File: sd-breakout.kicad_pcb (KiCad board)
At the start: 2 copper layers, 31.1 x 27.9 mm, 7 parts, among them J1 Header, J2 microSD Socket, U1 EClamp2410P

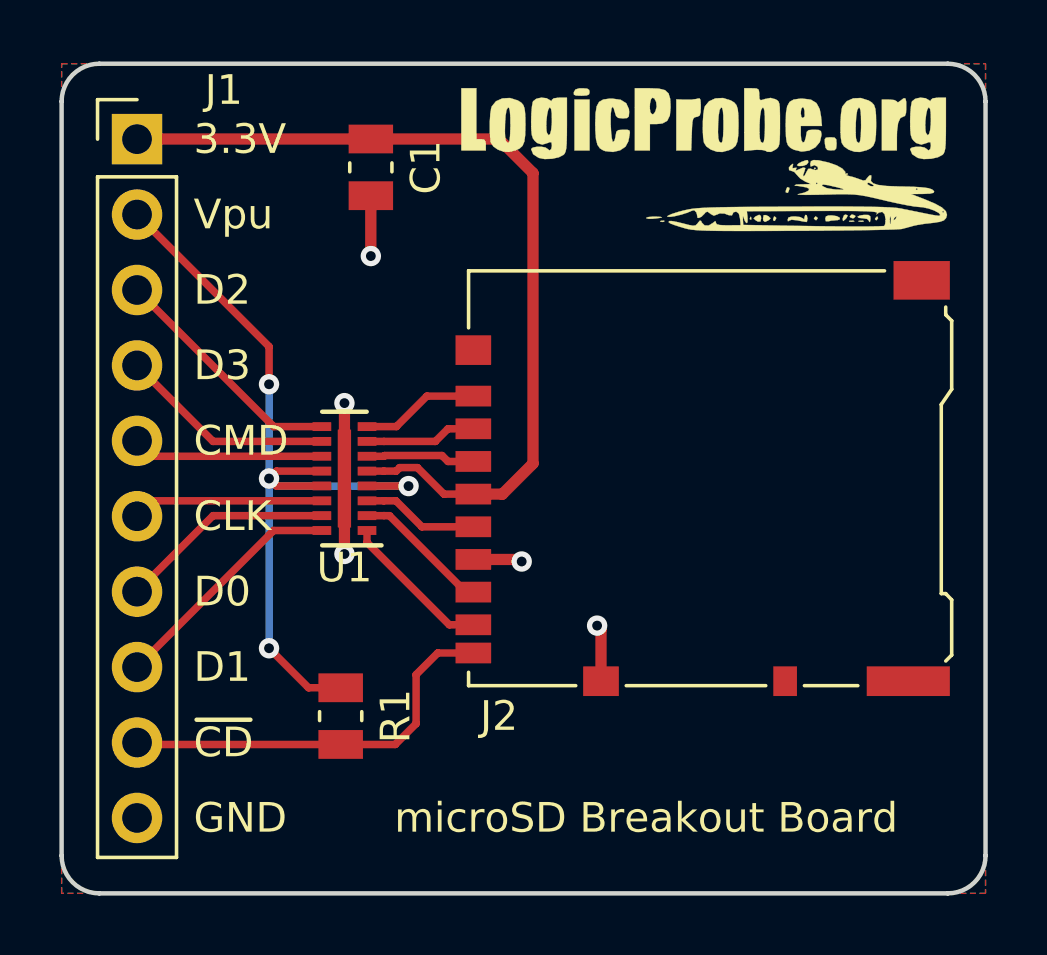
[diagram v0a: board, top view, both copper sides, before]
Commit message: Updated project to KiCad v6
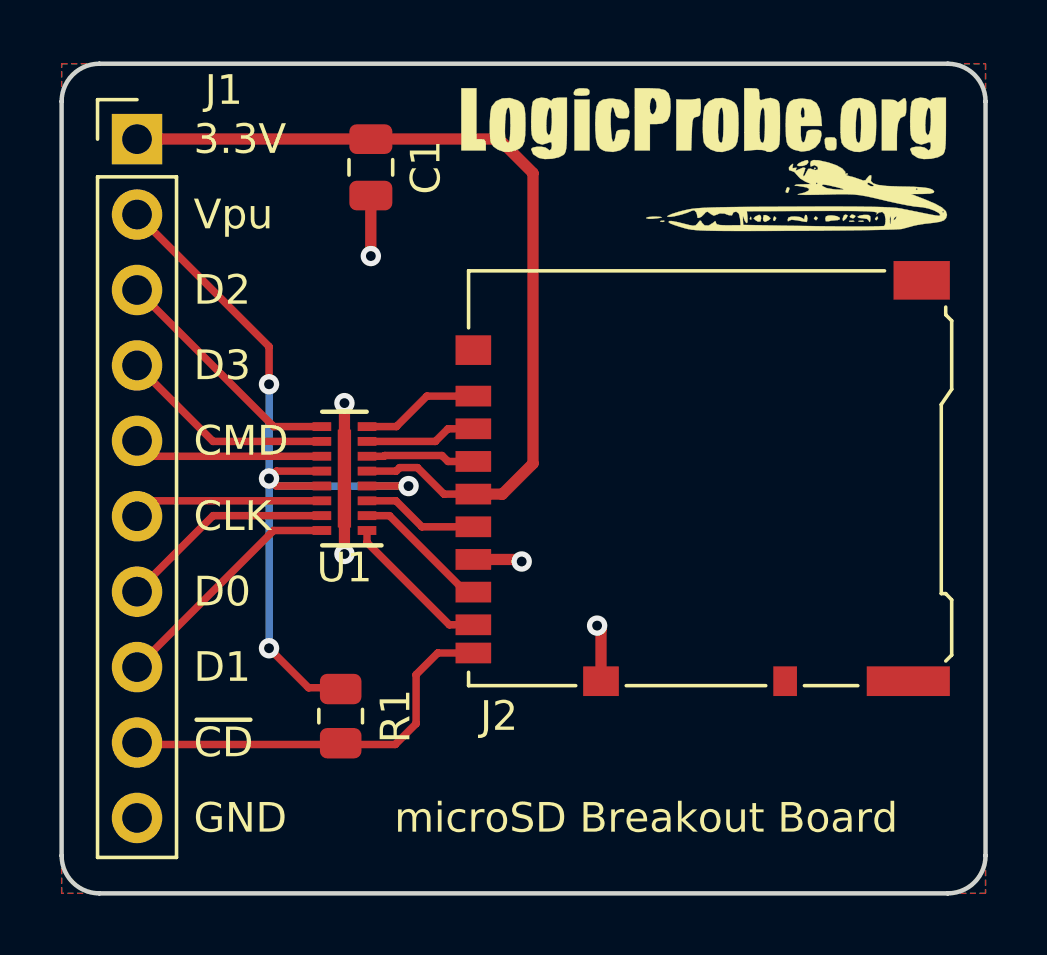
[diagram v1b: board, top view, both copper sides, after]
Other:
- net class Default removed
- board text added: "Rev: ${REVISION} ${ISSUE_DATE}"
- board text added: "~{CD}"
- board text removed: "Rev: A 2018-03-05"
- board text removed: "~CD"
